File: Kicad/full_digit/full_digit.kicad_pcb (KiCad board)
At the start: 2 copper layers, 106.7 x 152.4 mm, 51 parts, among them J1 CONN_8, J10 CONN_01X03, J11 CONN_01X12, J12 CONN_01X12, J13 CONN_01X08, J14 CONN_01X06, J15 CONN_01X10, J16 CONN_01X08, J17 CONN_01X17, J18 CONN_01X17, J19 RASM722X, J2 CONN_8, J3 CONN_8, J4 CONN_8, J5 CONN_8, J6 CONN_8, J7 CONN_8, J8 CONN_8, J9 CONN_01X03, U1 TLC5917, X1 MTHOLE, X2 MTHOLE, X3 MTHOLE, X4 MTHOLE

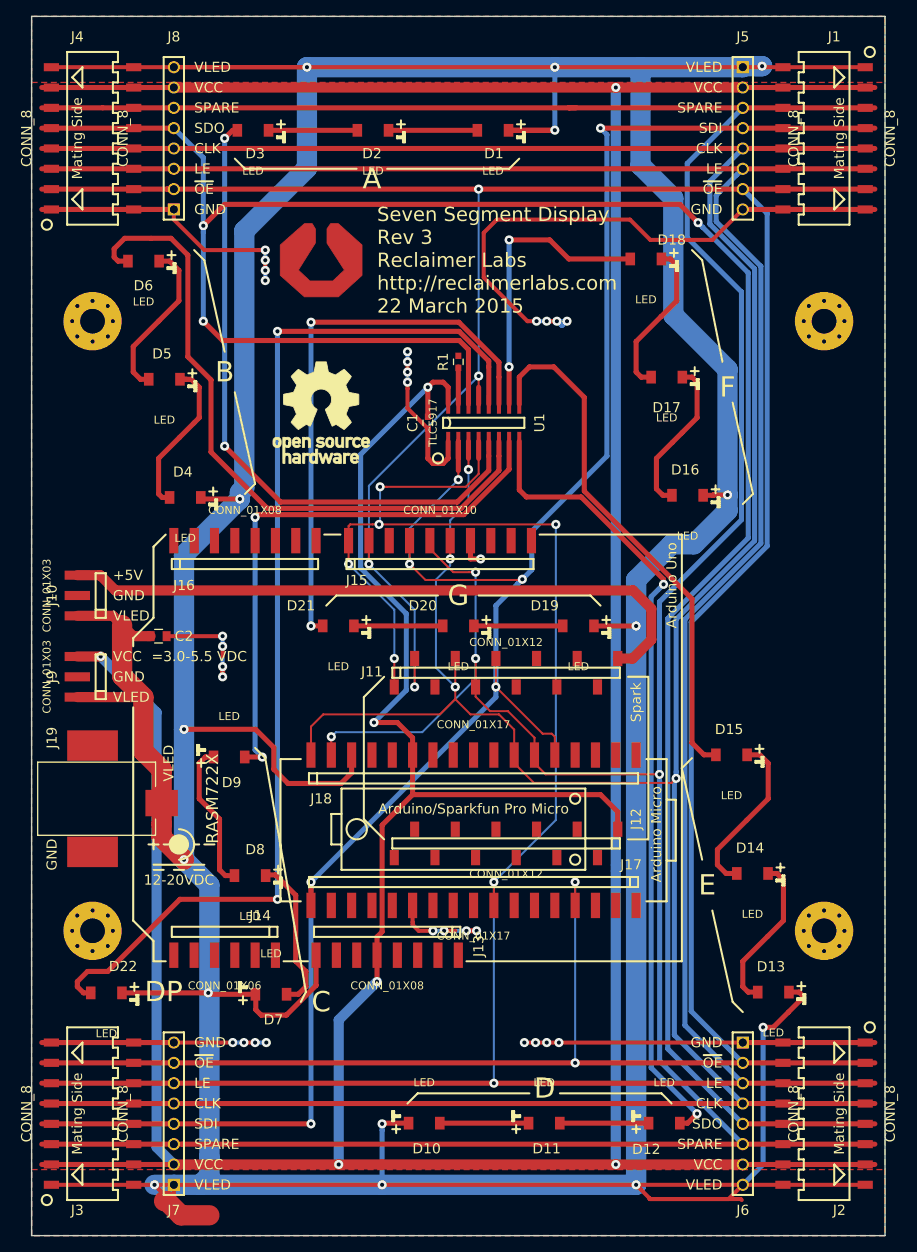
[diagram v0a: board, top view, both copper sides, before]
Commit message: Updated controller pads
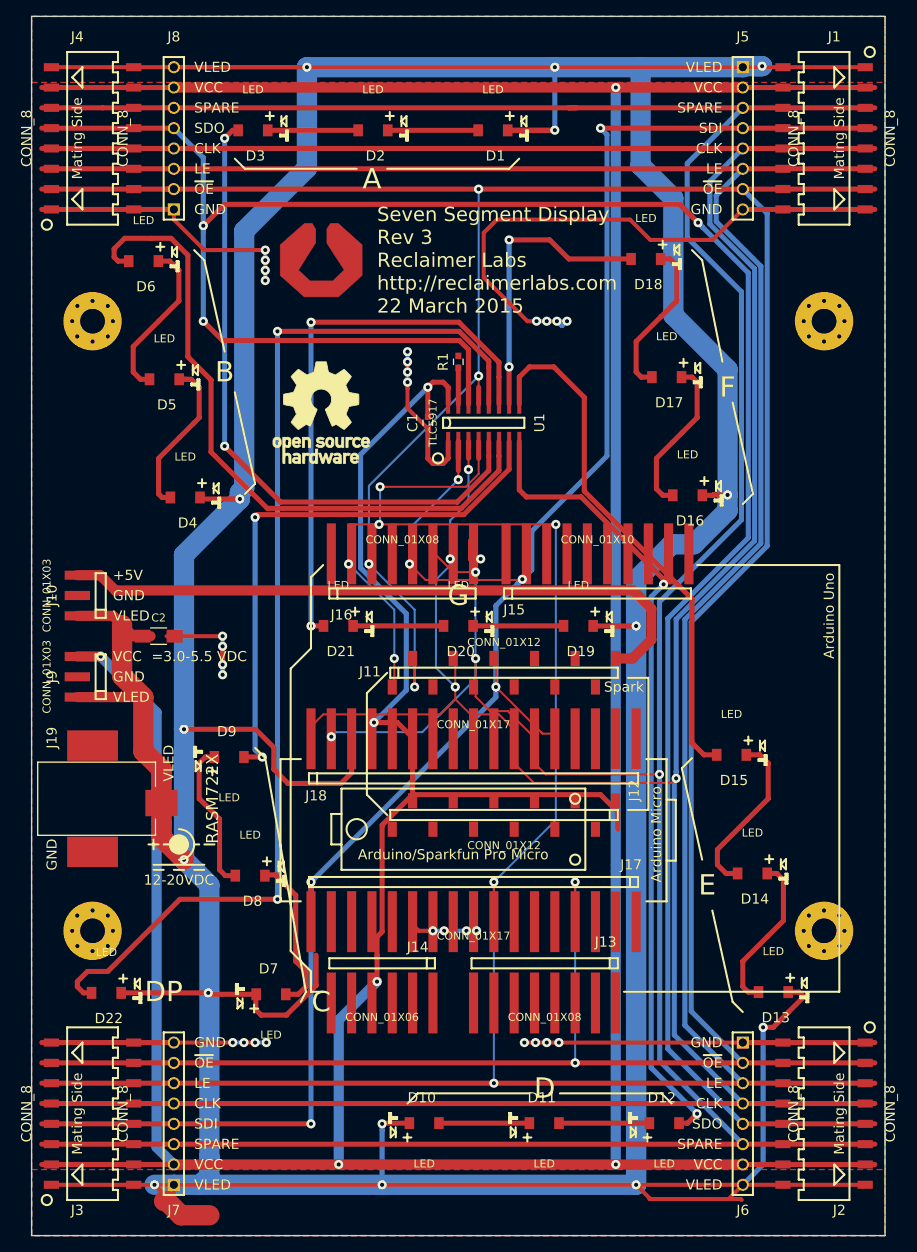
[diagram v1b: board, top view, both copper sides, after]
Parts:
- C2: footprint Capacitors_SMD:C_0805 -> Capacitors_SMD:C_1206_HandSoldering
- moved J13 20.1 mm to (132.7, 189.9)
- moved J14 20.1 mm to (112.4, 189.9)
- moved J16 20.0 mm to (114.9, 137.8)
- moved J15 20.0 mm to (139.3, 137.8)
- moved J12 3.57 mm to (127.6, 168.4)
- moved J11 0.25 mm to (127.6, 150.6)
- turned D1 to 0 degrees
- turned D10 to 180 degrees
- turned D11 to 180 degrees
- turned D12 to 180 degrees
- turned D13 to 0 degrees
- turned D14 to 0 degrees
- turned D15 to 0 degrees
- turned D16 to 0 degrees
- turned D17 to 0 degrees
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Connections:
- D1 pad 1: Vled -> Net-(D1-Pad1)
- D1 pad 2: Net-(D1-Pad2) -> Vled
- D10 pad 1: Vled -> Net-(D10-Pad1)
- D10 pad 2: Net-(D10-Pad2) -> Vled
- D11 pad 1: Net-(D10-Pad2) -> Net-(D11-Pad1)
- D11 pad 2: Net-(D11-Pad2) -> Net-(D10-Pad1)
- D12 pad 1: Net-(D11-Pad2) -> Net-(D12-Pad1)
- D12 pad 2: Net-(D12-Pad2) -> Net-(D11-Pad1)
- D13 pad 1: Vled -> Net-(D13-Pad1)
- D13 pad 2: Net-(D13-Pad2) -> Vled
- D14 pad 1: Net-(D13-Pad2) -> Net-(D14-Pad1)
- D14 pad 2: Net-(D14-Pad2) -> Net-(D13-Pad1)
- D15 pad 1: Net-(D14-Pad2) -> Net-(D15-Pad1)
- D15 pad 2: Net-(D15-Pad2) -> Net-(D14-Pad1)
- D16 pad 1: Vled -> Net-(D16-Pad1)
- D16 pad 2: Net-(D16-Pad2) -> Vled
- D17 pad 1: Net-(D16-Pad2) -> Net-(D17-Pad1)
- D17 pad 2: Net-(D17-Pad2) -> Net-(D16-Pad1)
- D18 pad 1: Net-(D17-Pad2) -> Net-(D18-Pad1)
- D18 pad 2: Net-(D18-Pad2) -> Net-(D17-Pad1)
- D19 pad 1: Vled -> Net-(D19-Pad1)
- D19 pad 2: Net-(D19-Pad2) -> Vled
- D2 pad 1: Net-(D1-Pad2) -> Net-(D2-Pad1)
- D2 pad 2: Net-(D2-Pad2) -> Net-(D1-Pad1)
- D20 pad 1: Net-(D19-Pad2) -> Net-(D20-Pad1)
- D20 pad 2: Net-(D20-Pad2) -> Net-(D19-Pad1)
- D21 pad 1: Net-(D20-Pad2) -> Net-(D21-Pad1)
- D21 pad 2: Net-(D21-Pad2) -> Net-(D20-Pad1)
- D22 pad 1: Vled -> Net-(D22-Pad1)
- D22 pad 2: Net-(D22-Pad2) -> Vled
- D3 pad 1: Net-(D2-Pad2) -> Net-(D3-Pad1)
- D3 pad 2: Net-(D3-Pad2) -> Net-(D2-Pad1)
- D4 pad 1: Vled -> Net-(D4-Pad1)
- D4 pad 2: Net-(D4-Pad2) -> Vled
- D5 pad 1: Net-(D4-Pad2) -> Net-(D5-Pad1)
- D5 pad 2: Net-(D5-Pad2) -> Net-(D4-Pad1)
- D6 pad 1: Net-(D5-Pad2) -> Net-(D6-Pad1)
- D6 pad 2: Net-(D6-Pad2) -> Net-(D5-Pad1)
- D7 pad 1: Vled -> Net-(D7-Pad1)
- D7 pad 2: Net-(D7-Pad2) -> Vled
- D8 pad 1: Net-(D7-Pad2) -> Net-(D8-Pad1)
- D8 pad 2: Net-(D8-Pad2) -> Net-(D7-Pad1)
- D9 pad 1: Net-(D8-Pad2) -> Net-(D9-Pad1)
- D9 pad 2: Net-(D9-Pad2) -> Net-(D8-Pad1)
- J19 pad 3: Net-(J19-Pad3) -> GND
- U1 pad 10: Net-(D18-Pad2) -> Net-(D18-Pad1)
- U1 pad 11: Net-(D21-Pad2) -> Net-(D21-Pad1)
- U1 pad 12: Net-(D22-Pad2) -> Net-(D22-Pad1)
- U1 pad 5: Net-(D3-Pad2) -> Net-(D3-Pad1)
- U1 pad 6: Net-(D6-Pad2) -> Net-(D6-Pad1)
- U1 pad 7: Net-(D9-Pad2) -> Net-(D9-Pad1)
- U1 pad 8: Net-(D12-Pad2) -> Net-(D12-Pad1)
- U1 pad 9: Net-(D15-Pad2) -> Net-(D15-Pad1)
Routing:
- net Net-(D22-Pad2): track 136.7 -> 0.00 mm, vias 2 -> 0
- net Net-(D22-Pad1): track 0.00 -> 136.7 mm, vias 0 -> 2
- net Net-(D12-Pad1): track 0.00 -> 101.2 mm, vias 0 -> 2
- net Net-(D12-Pad2): track 101.2 -> 0.00 mm, vias 2 -> 0
- net Net-(D6-Pad2): track 83.9 -> 0.00 mm
- net Net-(D6-Pad1): track 0.00 -> 83.9 mm
- net Net-(D3-Pad2): track 81.7 -> 0.00 mm, vias 2 -> 0
- net Net-(D3-Pad1): track 0.00 -> 81.7 mm, vias 0 -> 2
- net Net-(D21-Pad2): track 70.3 -> 0.00 mm, vias 2 -> 0
- net Net-(D21-Pad1): track 0.00 -> 70.3 mm, vias 0 -> 2
- net Net-(D9-Pad2): track 70.3 -> 0.00 mm, vias 2 -> 0
- net Net-(D9-Pad1): track 0.00 -> 70.3 mm, vias 0 -> 2
- net Net-(D15-Pad2): track 66.0 -> 0.00 mm
- net Net-(D15-Pad1): track 0.00 -> 66.0 mm
- net /LE: track 570.4 -> 517.2 mm, vias 7 -> 3
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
